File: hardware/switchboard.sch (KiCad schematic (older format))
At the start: 6 parts

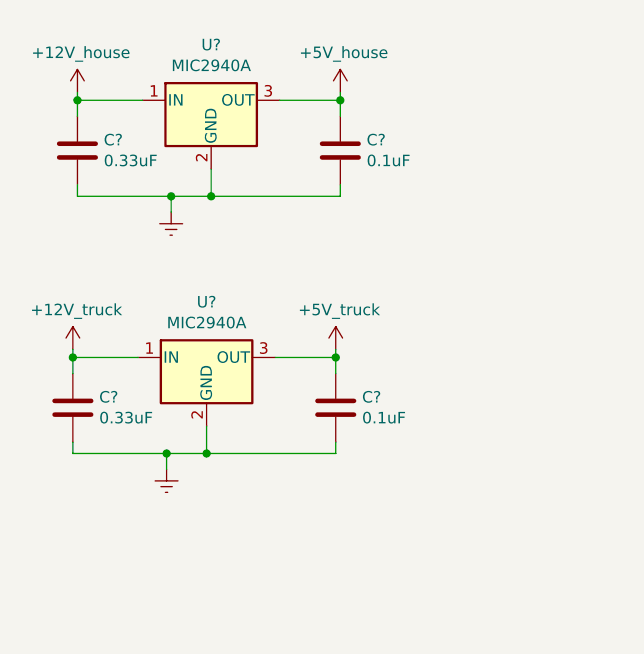
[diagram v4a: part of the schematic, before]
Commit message: hardware: change output stage of MIC2940A's
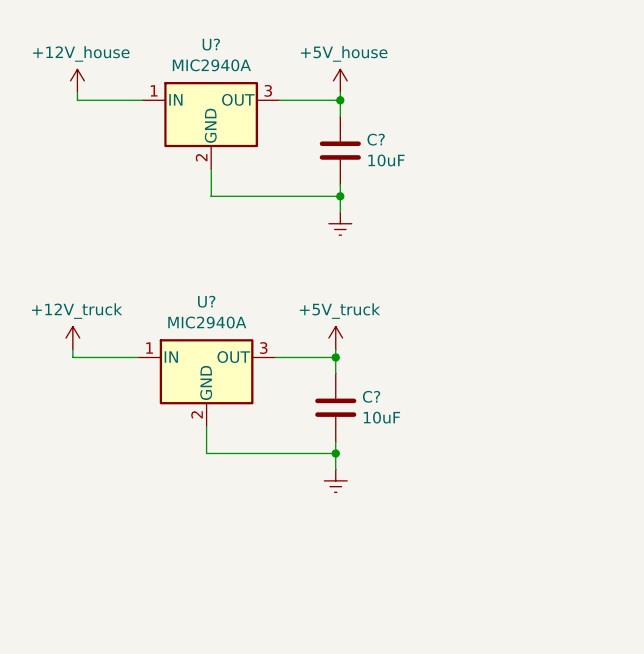
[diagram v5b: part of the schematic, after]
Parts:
- removed C? (x2): 0.33uF, Capacitor_SMD:C_0805_2012Metric_Pad1.18x1.45mm_HandSolder, symbol Device:C
- C? (x2): value 0.1uF -> 10uF
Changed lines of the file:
@@
-$Comp
-L Device:C C?
-U 1 1 60B4A4DB
-P 1115 1475
-AR Path="/605C1303/60B4A4DB" Ref="C?"  Part="1"
-AR Path="/60B4A4DB" Ref="C?"  Part="1"
-F 0 "C?" H 1230 1521 50  0000 L CNN
-F 1 "0.33uF" H 1230 1430 50  0000 L CNN
-F 2 "Capacitor_SMD:C_0805_2012Metric_Pad1.18x1.45mm_HandSolder" H 1153 1325 50  0001 C CNN
-F 3 "~" H 1115 1475 50  0001 C CNN
-	1    1115 1475
-	1    0    0    -1
-$EndComp
 $Comp
 L Device:C C?
@@
 AR Path="/60B4A4E1" Ref="C?"  Part="1"
 F 0 "C?" H 2380 1521 50  0000 L CNN
-F 1 "0.1uF" H 2380 1430 50  0000 L CNN
+F 1 "10uF" H 2380 1430 50  0000 L CNN
 F 2 "Capacitor_SMD:C_0805_2012Metric_Pad1.18x1.45mm_HandSolder" H 2303 1325 50  0001 C CNN
 F 3 "~" H 2265 1475 50  0001 C CNN
@@
 	1115 1255 1400 1255
 Wire Wire Line
-	1115 1625 1115 1675
-Wire Wire Line
-	1115 1675 1525 1675
-Wire Wire Line
 	2265 1675 2265 1625
-Connection ~ 1700 1675
 Wire Wire Line
 	1700 1675 2265 1675
@@
 L power:GNDREF #PWR?
 U 1 1 60B4A4EE
-P 1525 1745
+P 2265 1745
 AR Path="/605C1303/60B4A4EE" Ref="#PWR?"  Part="1"
 AR Path="/60B4A4EE" Ref="#PWR?"  Part="1"
-F 0 "#PWR?" H 1525 1495 50  0001 C CNN
-F 1 "GNDREF" H 1530 1572 50  0001 C CNN
-F 2 "" H 1525 1745 50  0001 C CNN
-F 3 "" H 1525 1745 50  0001 C CNN
-	1    1525 1745
+F 0 "#PWR?" H 2265 1495 50  0001 C CNN
+F 1 "GNDREF" H 2270 1572 50  0001 C CNN
+F 2 "" H 2265 1745 50  0001 C CNN
+F 3 "" H 2265 1745 50  0001 C CNN
+	1    2265 1745
 	1    0    0    -1
 $EndComp
 Wire Wire Line
-	1525 1745 1525 1675
-Connection ~ 1525 1675
-Wire Wire Line
-	1525 1675 1700 1675
+	2265 1745 2265 1675
 Wire Wire Line
 	1700 1555 1700 1675
-Wire Wire Line
-	1115 1255 1115 1325
 Wire Wire Line
 	2265 1255 2265 1325
@@
 Wire Wire Line
 	1115 1255 1115 1220
-Connection ~ 1115 1255
 $Comp
 L switchboard:+12V_house #PWR?
@@
 $Comp
 L Device:C C?
-U 1 1 60B50BC1
-P 1095 2600
-AR Path="/605C1303/60B50BC1" Ref="C?"  Part="1"
-AR Path="/60B50BC1" Ref="C?"  Part="1"
-F 0 "C?" H 1210 2646 50  0000 L CNN
-F 1 "0.33uF" H 1210 2555 50  0000 L CNN
-F 2 "Capacitor_SMD:C_0805_2012Metric_Pad1.18x1.45mm_HandSolder" H 1133 2450 50  0001 C CNN
-F 3 "~" H 1095 2600 50  0001 C CNN
-	1    1095 2600
-	1    0    0    -1
-$EndComp
-$Comp
-L Device:C C?
 U 1 1 60B50BC7
 P 2245 2600
@@
 AR Path="/60B50BC7" Ref="C?"  Part="1"
 F 0 "C?" H 2360 2646 50  0000 L CNN
-F 1 "0.1uF" H 2360 2555 50  0000 L CNN
+F 1 "10uF" H 2360 2555 50  0000 L CNN
 F 2 "Capacitor_SMD:C_0805_2012Metric_Pad1.18x1.45mm_HandSolder" H 2283 2450 50  0001 C CNN
 F 3 "~" H 2245 2600 50  0001 C CNN
@@
 	1095 2380 1380 2380
 Wire Wire Line
-	1095 2750 1095 2800
-Wire Wire Line
-	1095 2800 1505 2800
-Wire Wire Line
 	2245 2800 2245 2750
-Connection ~ 1680 2800
 Wire Wire Line
 	1680 2800 2245 2800
@@
 L power:GNDREF #PWR?
 U 1 1 60B50BD4
-P 1505 2870
+P 2245 2870
 AR Path="/605C1303/60B50BD4" Ref="#PWR?"  Part="1"
 AR Path="/60B50BD4" Ref="#PWR?"  Part="1"
-F 0 "#PWR?" H 1505 2620 50  0001 C CNN
-F 1 "GNDREF" H 1510 2697 50  0001 C CNN
-F 2 "" H 1505 2870 50  0001 C CNN
-F 3 "" H 1505 2870 50  0001 C CNN
-	1    1505 2870
+F 0 "#PWR?" H 2245 2620 50  0001 C CNN
+F 1 "GNDREF" H 2250 2697 50  0001 C CNN
+F 2 "" H 2245 2870 50  0001 C CNN
+F 3 "" H 2245 2870 50  0001 C CNN
+	1    2245 2870
 	1    0    0    -1
 $EndComp
 Wire Wire Line
-	1505 2870 1505 2800
-Connection ~ 1505 2800
-Wire Wire Line
-	1505 2800 1680 2800
+	2245 2870 2245 2800
 Wire Wire Line
 	1680 2680 1680 2800
-Wire Wire Line
-	1095 2380 1095 2450
 Wire Wire Line
 	2245 2380 2245 2450
@@
 Wire Wire Line
 	1095 2380 1095 2345
-Connection ~ 1095 2380
 $Comp
 L switchboard:+5V_house #PWR?
@@
 	1    0    0    -1
 $EndComp
+Connection ~ 2245 2800
+Connection ~ 2265 1675
 $EndSCHEMATC

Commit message: hardware: use appropriate bypass caps on MIC2940A
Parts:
- removed C? (x2): 10uF, Capacitor_SMD:C_0805_2012Metric_Pad1.18x1.45mm_HandSolder, symbol Device:C
- added C? (x2): 10uF, symbol Device:CP1
- added C? (x2): 0.22uF, symbol Device:C
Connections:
- net +12V: now also C?.1, C?.1
- net +5V: now also C?.1, C?.1
- net GNDREF: now also C?.2, C?.2, C?.2, C?.2
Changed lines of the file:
@@
 Wire Bus Line
 	12425 8055 11020 8055
-$Comp
-L Device:C C?
-U 1 1 60B4A4E1
-P 2265 1475
-AR Path="/605C1303/60B4A4E1" Ref="C?"  Part="1"
-AR Path="/60B4A4E1" Ref="C?"  Part="1"
-F 0 "C?" H 2380 1521 50  0000 L CNN
-F 1 "10uF" H 2380 1430 50  0000 L CNN
-F 2 "Capacitor_SMD:C_0805_2012Metric_Pad1.18x1.45mm_HandSolder" H 2303 1325 50  0001 C CNN
-F 3 "~" H 2265 1475 50  0001 C CNN
-	1    2265 1475
-	1    0    0    -1
-$EndComp
 Wire Wire Line
 	2000 1255 2265 1255
 Wire Wire Line
-	1115 1255 1400 1255
+	1115 1255 1240 1255
 Wire Wire Line
 	2265 1675 2265 1625
@@
 	1    0    0    -1
 $EndComp
-$Comp
-L Device:C C?
-U 1 1 60B50BC7
-P 2245 2600
-AR Path="/605C1303/60B50BC7" Ref="C?"  Part="1"
-AR Path="/60B50BC7" Ref="C?"  Part="1"
-F 0 "C?" H 2360 2646 50  0000 L CNN
-F 1 "10uF" H 2360 2555 50  0000 L CNN
-F 2 "Capacitor_SMD:C_0805_2012Metric_Pad1.18x1.45mm_HandSolder" H 2283 2450 50  0001 C CNN
-F 3 "~" H 2245 2600 50  0001 C CNN
-	1    2245 2600
-	1    0    0    -1
-$EndComp
 Wire Wire Line
 	1980 2380 2245 2380
 Wire Wire Line
-	1095 2380 1380 2380
+	1095 2380 1230 2380
 Wire Wire Line
 	2245 2800 2245 2750
@@
 F82 "REAR_LOW_CURB_CTRL_12V" I L 8820 7695 50
 $EndSheet
+$Comp
+L Device:CP1 C?
+U 1 1 675D6C9F
+P 2245 2600
+F 0 "C?" H 2360 2646 50  0000 L CNN
+F 1 "10uF" H 2360 2555 50  0000 L CNN
+F 2 "" H 2245 2600 50  0001 C CNN
+F 3 "~" H 2245 2600 50  0001 C CNN
+	1    2245 2600
+	1    0    0    -1
+$EndComp
+$Comp
+L Device:CP1 C?
+U 1 1 675D9186
+P 2265 1475
+F 0 "C?" H 2380 1521 50  0000 L CNN
+F 1 "10uF" H 2380 1430 50  0000 L CNN
+F 2 "" H 2265 1475 50  0001 C CNN
+F 3 "~" H 2265 1475 50  0001 C CNN
+	1    2265 1475
+	1    0    0    -1
+$EndComp
+$Comp
+L Device:C C?
+U 1 1 675DC63E
+P 1240 1475
+F 0 "C?" H 1355 1521 50  0000 L CNN
+F 1 "0.22uF" H 1355 1430 50  0000 L CNN
+F 2 "" H 1278 1325 50  0001 C CNN
+F 3 "~" H 1240 1475 50  0001 C CNN
+	1    1240 1475
+	1    0    0    -1
+$EndComp
+$Comp
+L Device:C C?
+U 1 1 675DD670
+P 1230 2585
+F 0 "C?" H 1345 2631 50  0000 L CNN
+F 1 "0.22uF" H 1345 2540 50  0000 L CNN
+F 2 "" H 1268 2435 50  0001 C CNN
+F 3 "~" H 1230 2585 50  0001 C CNN
+	1    1230 2585
+	1    0    0    -1
+$EndComp
+Wire Wire Line
+	1700 1675 1240 1675
+Wire Wire Line
+	1240 1675 1240 1625
+Connection ~ 1700 1675
+Wire Wire Line
+	1240 1325 1240 1255
+Connection ~ 1240 1255
+Wire Wire Line
+	1240 1255 1400 1255
+Wire Wire Line
+	1230 2435 1230 2380
+Connection ~ 1230 2380
+Wire Wire Line
+	1230 2380 1380 2380
+Wire Wire Line
+	1680 2800 1230 2800
+Wire Wire Line
+	1230 2800 1230 2735
+Connection ~ 1680 2800
 $EndSCHEMATC
